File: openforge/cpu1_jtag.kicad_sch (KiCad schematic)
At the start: 47 parts, among them P2 Heaader 2x10 1.27mm, U16 74LVC1G07, U3 74LVC1G06, U5 AM3352BZCZ100, U6 SN74LVC1G74DCTR, Y1 32.768K/12.5p, Y2 24MHz/20p, Y4 ASCO

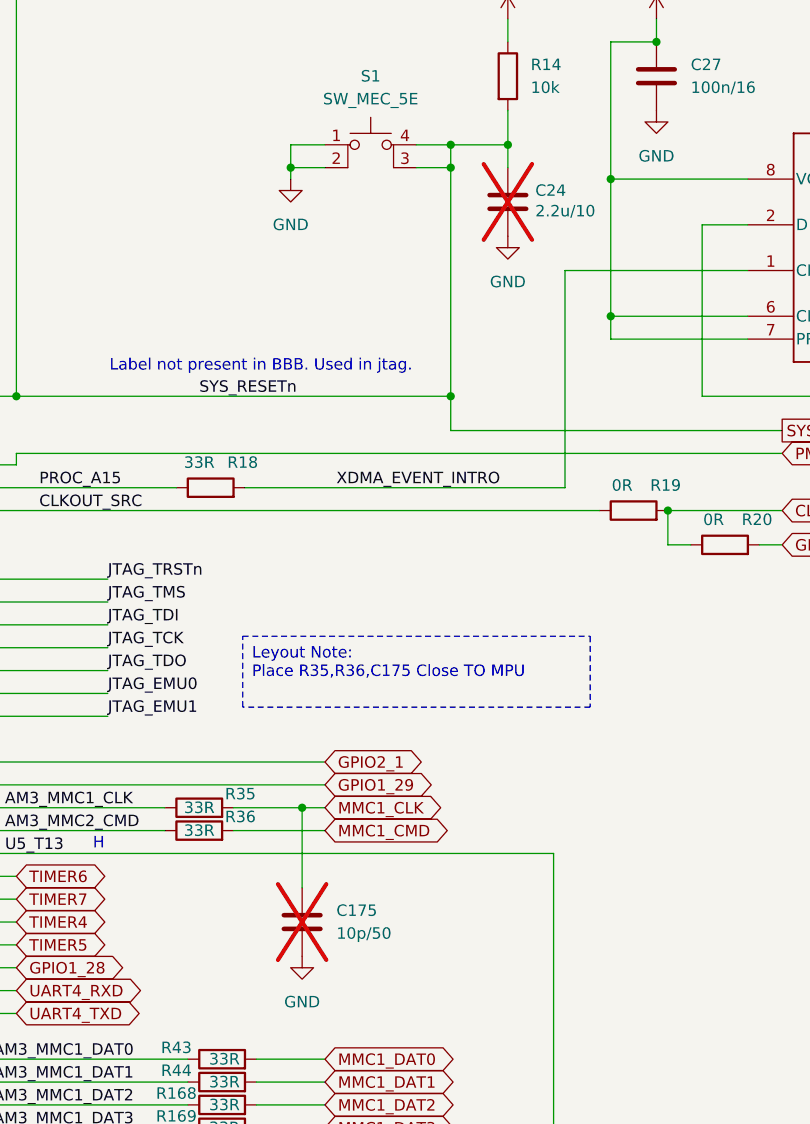
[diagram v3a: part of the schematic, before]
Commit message: fixed all errors and major warnings
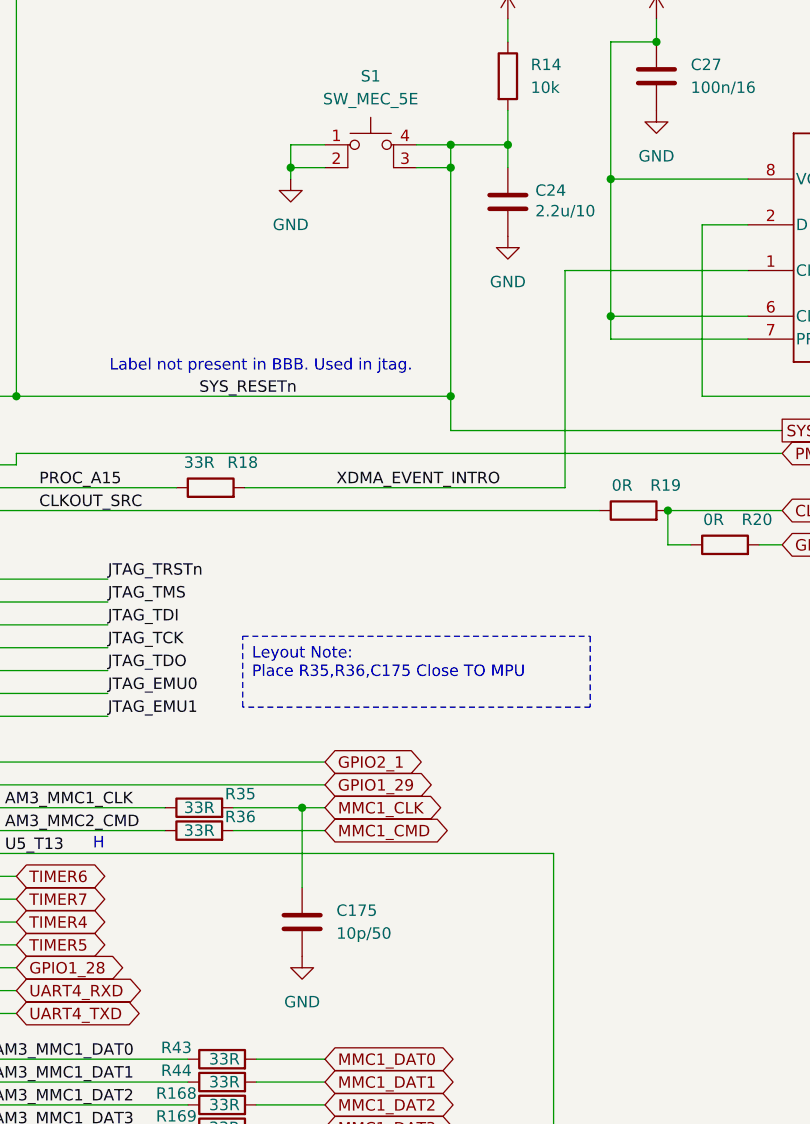
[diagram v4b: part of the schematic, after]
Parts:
- C158, C159, C21, C22, C25, C26, C27, C28, C29, C30: footprint Capacitor_SMD:C_0402_1005Metric -> footprints:C_0402_1005Metric
- C175, C24: footprint Capacitor_SMD:C_0402_1005Metric -> footprints:C_0402_1005Metric; now fitted
- R14, R160, R161, R162, R167, R168, R169, R17, R170, R171, R172, R173, R18, R19, R20, R21, R22, R23, R24, R25, R29, R30, R35, R36, R43, R44: footprint Resistor_SMD:R_0402_1005Metric -> footprints:R_0402_1005Metric
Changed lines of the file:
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@@
 			)
 		)
-		(property "Footprint" "Resistor_SMD:R_0402_1005Metric"
+		(property "Footprint" "footprints:R_0402_1005Metric"
 			(at 400.05 283.718 90)
 			(effects
@@
 			)
 		)
-		(property "Footprint" "Resistor_SMD:R_0402_1005Metric"
+		(property "Footprint" "footprints:R_0402_1005Metric"
 			(at 326.39 175.768 90)
 			(effects
@@
 			)
 		)
-		(property "Footprint" "Resistor_SMD:R_0402_1005Metric"
+		(property "Footprint" "footprints:R_0402_1005Metric"
 			(at 356.362 54.61 90)
 			(effects
@@
 			)
 		)
-		(property "Footprint" "Capacitor_SMD:C_0402_1005Metric"
+		(property "Footprint" "footprints:C_0402_1005Metric"
 			(at 151.4348 93.98 0)
 			(effects
@@
 			)
 		)
-		(property "Footprint" "Resistor_SMD:R_0402_1005Metric"
+		(property "Footprint" "footprints:R_0402_1005Metric"
 			(at 211.582 269.24 90)
 			(effects
@@
 			)
 		)
-		(property "Footprint" "Capacitor_SMD:C_0402_1005Metric"
+		(property "Footprint" "footprints:C_0402_1005Metric"
 			(at 389.89 268.2748 0)
 			(effects
@@
 			)
 		)
-		(property "Footprint" "Capacitor_SMD:C_0402_1005Metric"
+		(property "Footprint" "footprints:C_0402_1005Metric"
 			(at 211.1248 369.57 0)
 			(effects
@@
 			)
 		)
-		(property "Footprint" "Resistor_SMD:R_0402_1005Metric"
+		(property "Footprint" "footprints:R_0402_1005Metric"
 			(at 323.85 140.208 90)
 			(effects
@@
 			)
 		)
-		(property "Footprint" "Capacitor_SMD:C_0402_1005Metric"
+		(property "Footprint" "footprints:C_0402_1005Metric"
 			(at 375.6152 58.42 0)
 			(effects
@@
 			)
 		)
-		(property "Footprint" "Resistor_SMD:R_0402_1005Metric"
+		(property "Footprint" "footprints:R_0402_1005Metric"
 			(at 400.05 244.348 90)
 			(effects
@@
 			)
 		)
-		(property "Footprint" "Resistor_SMD:R_0402_1005Metric"
+		(property "Footprint" "footprints:R_0402_1005Metric"
 			(at 326.39 183.388 90)
 			(effects
@@
 			)
 		)
-		(property "Footprint" "Resistor_SMD:R_0402_1005Metric"
+		(property "Footprint" "footprints:R_0402_1005Metric"
 			(at 325.12 102.108 90)
 			(effects
@@
 			)
 		)
-		(property "Footprint" "Resistor_SMD:R_0402_1005Metric"
+		(property "Footprint" "footprints:R_0402_1005Metric"
 			(at 272.542 374.65 90)
 			(effects
@@
 			)
 		)
-		(property "Footprint" "Resistor_SMD:R_0402_1005Metric"
+		(property "Footprint" "footprints:R_0402_1005Metric"
 			(at 326.39 180.848 90)
 			(effects
@@
 			)
 		)
-		(property "Footprint" "Resistor_SMD:R_0402_1005Metric"
+		(property "Footprint" "footprints:R_0402_1005Metric"
 			(at 326.39 178.308 90)
 			(effects
@@
 			)
 		)
-		(property "Footprint" "Resistor_SMD:R_0402_1005Metric"
+		(property "Footprint" "footprints:R_0402_1005Metric"
 			(at 373.38 199.898 90)
 			(effects
@@
 			)
 		)
-		(property "Footprint" "Resistor_SMD:R_0402_1005Metric"
+		(property "Footprint" "footprints:R_0402_1005Metric"
 			(at 429.26 70.358 90)
 			(effects
@@
 			)
 		)
-		(property "Footprint" "Resistor_SMD:R_0402_1005Metric"
+		(property "Footprint" "footprints:R_0402_1005Metric"
 			(at 326.39 168.148 90)
 			(effects
@@
 			)
 		)
-		(property "Footprint" "Resistor_SMD:R_0402_1005Metric"
+		(property "Footprint" "footprints:R_0402_1005Metric"
 			(at 138.938 107.95 90)
 			(effects
@@
 			)
 		)
-		(property "Footprint" "Resistor_SMD:R_0402_1005Metric"
+		(property "Footprint" "footprints:R_0402_1005Metric"
 			(at 326.39 170.688 90)
 			(effects
@@
 			)
 		)
-		(property "Footprint" "Capacitor_SMD:C_0402_1005Metric"
+		(property "Footprint" "footprints:C_0402_1005Metric"
 			(at 389.89 225.0948 0)
 			(effects
@@
 		(in_bom yes)
 		(on_board yes)
-		(dnp yes)
+		(dnp no)
 		(property "Reference" "C24"
 			(at 361.188 67.31 0)
@@
 			)
 		)
-		(property "Footprint" "Capacitor_SMD:C_0402_1005Metric"
+		(property "Footprint" "footprints:C_0402_1005Metric"
 			(at 359.1052 72.39 0)
 			(effects
@@
 			)
 		)
-		(property "Footprint" "Capacitor_SMD:C_0402_1005Metric"
+		(property "Footprint" "footprints:C_0402_1005Metric"
 			(at 201.6252 273.05 0)
 			(effects
@@
 			)
 		)
-		(property "Footprint" "Resistor_SMD:R_0402_1005Metric"
+		(property "Footprint" "footprints:R_0402_1005Metric"
 			(at 372.11 104.648 90)
 			(effects
@@
 			)
 		)
-		(property "Footprint" "Capacitor_SMD:C_0402_1005Metric"
+		(property "Footprint" "footprints:C_0402_1005Metric"
 			(at 191.77 72.6948 0)
 			(effects
@@
 		(in_bom yes)
 		(on_board yes)
-		(dnp yes)
+		(dnp no)
 		(fields_autoplaced yes)
 		(property "Reference" "C175"
@@
 			)
 		)
-		(property "Footprint" "Capacitor_SMD:C_0402_1005Metric"
+		(property "Footprint" "footprints:C_0402_1005Metric"
 			(at 336.2452 152.4 0)
 			(effects
@@
 			)
 		)
-		(property "Footprint" "Resistor_SMD:R_0402_1005Metric"
+		(property "Footprint" "footprints:R_0402_1005Metric"
 			(at 295.402 345.44 90)
 			(effects
@@
 			)
 		)
-		(property "Footprint" "Resistor_SMD:R_0402_1005Metric"
+		(property "Footprint" "footprints:R_0402_1005Metric"
 			(at 323.85 137.668 90)
 			(effects
@@
 			)
 		)
-		(property "Footprint" "Resistor_SMD:R_0402_1005Metric"
+		(property "Footprint" "footprints:R_0402_1005Metric"
 			(at 210.312 345.44 90)
 			(effects
@@
 			)
 		)
-		(property "Footprint" "Resistor_SMD:R_0402_1005Metric"
+		(property "Footprint" "footprints:R_0402_1005Metric"
 			(at 326.39 165.608 90)
 			(effects
@@
 			)
 		)
-		(property "Footprint" "Resistor_SMD:R_0402_1005Metric"
+		(property "Footprint" "footprints:R_0402_1005Metric"
 			(at 164.338 82.55 90)
 			(effects
@@
 			)
 		)
-		(property "Footprint" "Capacitor_SMD:C_0402_1005Metric"
+		(property "Footprint" "footprints:C_0402_1005Metric"
 			(at 136.1948 86.36 0)
 			(effects
@@
 			)
 		)
-		(property "Footprint" "Resistor_SMD:R_0402_1005Metric"
+		(property "Footprint" "footprints:R_0402_1005Metric"
 			(at 173.99 60.198 90)
 			(effects
@@
 			)
 		)
-		(property "Footprint" "Resistor_SMD:R_0402_1005Metric"
+		(property "Footprint" "footprints:R_0402_1005Metric"
 			(at 326.39 173.228 90)
 			(effects
@@
 			)
 		)
-		(property "Footprint" "Resistor_SMD:R_0402_1005Metric"
+		(property "Footprint" "footprints:R_0402_1005Metric"
 			(at 382.27 108.458 90)
 			(effects
@@
 			)
 		)
-		(property "Footprint" "Capacitor_SMD:C_0402_1005Metric"
+		(property "Footprint" "footprints:C_0402_1005Metric"
 			(at 191.77 57.4548 0)
 			(effects
@@
 			)
 		)
-		(property "Footprint" "Capacitor_SMD:C_0402_1005Metric"
+		(property "Footprint" "footprints:C_0402_1005Metric"
 			(at 242.8748 369.57 0)
 			(effects
@@
 			)
 		)
-		(property "Footprint" "Resistor_SMD:R_0402_1005Metric"
+		(property "Footprint" "footprints:R_0402_1005Metric"
 			(at 373.38 208.788 90)
 			(effects
